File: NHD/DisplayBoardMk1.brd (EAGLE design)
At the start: 95.2 x 82.5 mm, 21 parts, among them K1 AQH2223

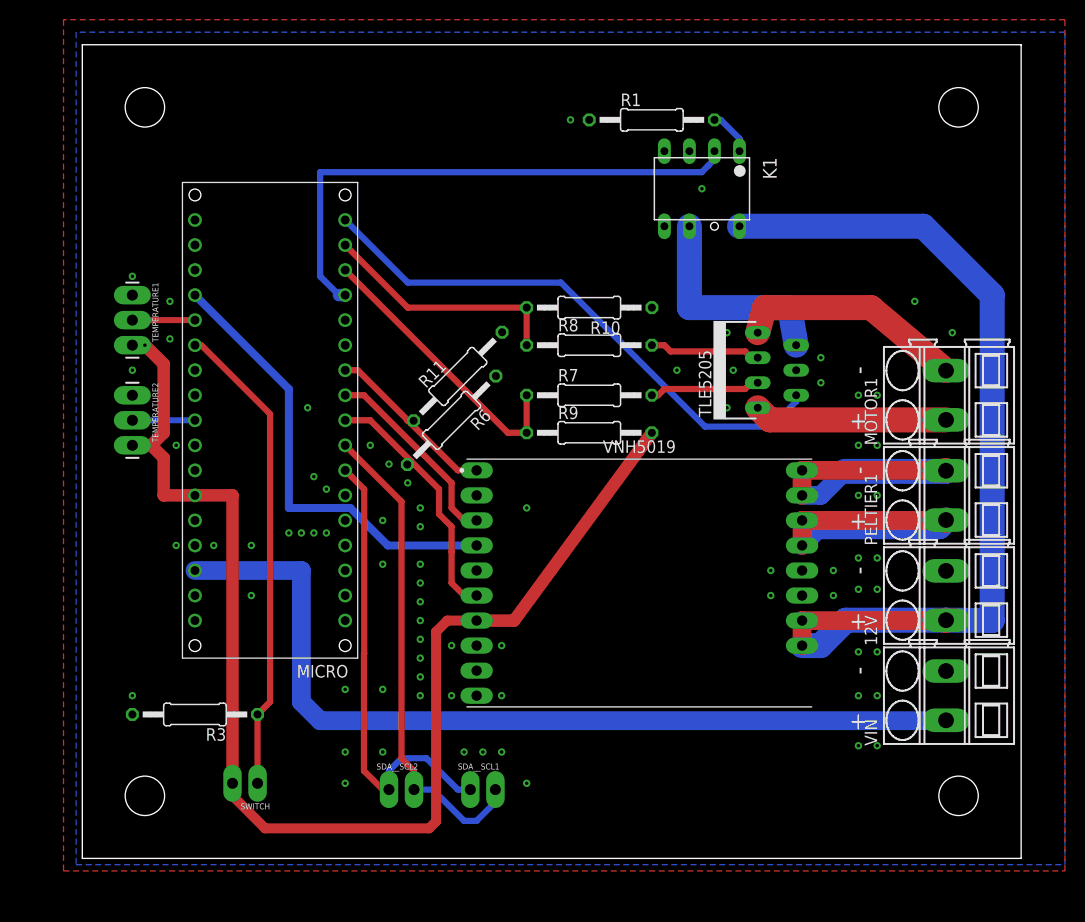
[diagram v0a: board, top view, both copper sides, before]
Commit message: Display Board. Attained old board files. Schematic organization.
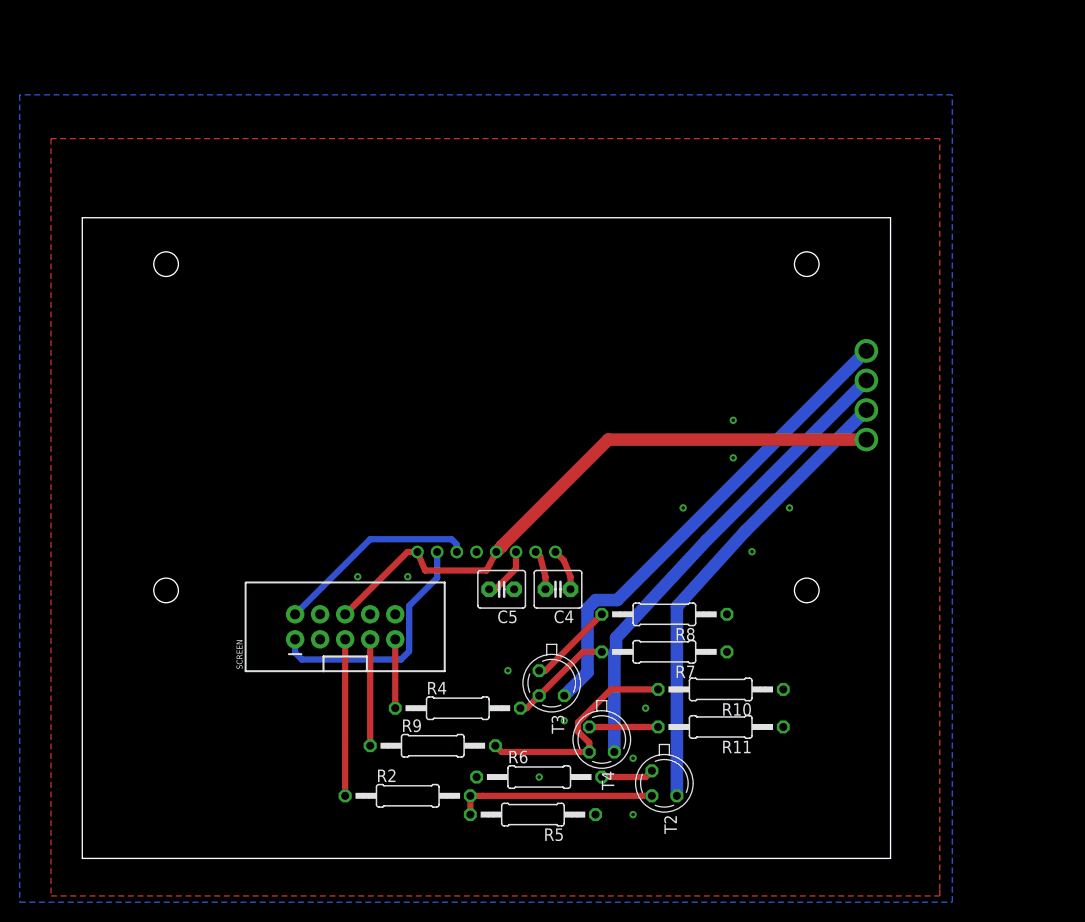
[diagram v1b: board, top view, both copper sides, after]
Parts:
- removed 12V, MOTOR1, PELTIER1, VIN: SMKDSP_1,5/2, con-phoenix-smkdsp:SMKDSP_1,5/2
- removed K1: AQH2223, relay:DIL07
- removed MICRO: ARDUINO_MICROFOOTPRINT, arduino-micro:ARDUINO-MICRO
- removed R1: 220, resistor:0207/12
- removed R3: 4.7k, resistor:0207/12
- removed SDA__SCL1, SDA__SCL2, SWITCH: (no value), SparkFun-Connectors:1X02_LONGPADS
- removed TEMPERATURE1, TEMPERATURE2: (no value), SparkFun-Connectors:1X03_LONGPADS
- removed TLE5205: TLE5205-2, infineon:P-TO220-7-11
- removed VNH5019: VNH5019VNH5019BOARD, GEMS:DIP3302W60P254L2400H500Q20B
- added C4, C5: 0.1uf, capacitor-wima:C2.5-4
- added R2, R4: 1k, resistor:0207/12
- added R5: 47k, resistor:0207/12
- added SCREEN: (no value), SparkFun-Connectors:2X5-SHROUDED
- added T2, T3, T4: 2N2222, transistor:TO18
- added U4: NHD‐C0220, GEMS:NHD-C0220
- R11, R6: value 47k -> 36
- R7: value 1k -> 47k
- R8: value 1k -> 36
- R9: value 47k -> 1k
- moved R11 44.4 mm to (64.8, 13.3), turned to 180 degrees
- moved R10 41.0 mm to (64.8, 17.1)
- moved R6 37.3 mm to (46.4, 8.26), turned to 0 degrees
- moved R9 35.5 mm to (35.6, 11.4)
- moved R8 28.3 mm to (59.1, 24.8), turned to 180 degrees
- moved R7 27.1 mm to (59.1, 21.0), turned to 180 degrees
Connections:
- removed net +12V: 12V.1, K1.8, VNH5019.VIN1, VNH5019.VIN2
- removed net +5V: MICRO.5V, R9.2, SWITCH.2, TEMPERATURE1.3, TEMPERATURE2.3, VNH5019.VDD
- removed net DOORSWITCH: MICRO.A2, R3.1, SWITCH.1
- removed net IN1: R7.2, TLE5205.3
- removed net IN2: R8.2, TLE5205.5
- removed net MOTOR-ENABLE: K1.2, MICRO.D9
- removed net MOTOR-ERRORFLAG: MICRO.D12, TLE5205.2
- removed net MOTOR-IN1: MICRO.D10, R7.1, R9.1
- removed net MOTOR-IN2: MICRO.D11, R10.2, R8.1
- removed net MOTOR-OUT1: MOTOR1.1, TLE5205.1
- removed net MOTOR-OUT2: MOTOR1.2, TLE5205.7
- removed net PELTIER-CURRENT: MICRO.A0, VNH5019.CS
- removed net PELTIER-INA: MICRO.D6, R11.1, VNH5019.INA
- removed net PELTIER-INB: MICRO.D4, R6.2, VNH5019.INB
- removed net PELTIER-OUTA: PELTIER1.2, VNH5019.OUTA1, VNH5019.OUTA2
- removed net PELTIER-OUTB: PELTIER1.1, VNH5019.OUTB1, VNH5019.OUTB2
- removed net PELTIER-PWM: MICRO.D5, VNH5019.PWM
- removed net POST-OPTO-DIODE: K1.1, R1.2
- removed net RELAY-TO-MOTORCONTROLLER: K1.6, TLE5205.6
- removed net SCL: MICRO.D3, SDA__SCL1.2, SDA__SCL2.2
- removed net SDA: MICRO.D2, SDA__SCL1.1, SDA__SCL2.1
- removed net TEMPERATURE1: MICRO.A1, TEMPERATURE1.2
- removed net TEMPERATURE2: MICRO.A5, TEMPERATURE2.2
- removed net VIN: MICRO.VIN, VIN.1
- new net 3V3: SCREEN.6, U4.1, U4.5, U4.A
- new net BLUE-NPN-BASE: R2.2, R5.2, T2.2
- new net BLUE-NPN-EMITTER: R6.2, T2.1
- new net GREEN-NPN-BASE: R10.2, R9.2, T4.2
- new net GREEN-NPN-EMITTER: R11.2, T4.1
- new net N$3: C5.2, U4.6
- new net RED-NPN-BASE: R4.2, R7.2, T3.2
- new net RED-NPN-EMITTER: R8.2, T3.1
- new net SCREEN-BLUE: T2.3, U4.BK
- new net SCREEN-BLUE-CONTROL: R2.1, SCREEN.5
- new net SCREEN-GREEN: T4.3, U4.GK
- new net SCREEN-GREEN-CONTROL: R9.1, SCREEN.7
- new net SCREEN-RED: T3.3, U4.RK
- new net SCREEN-RED-CONTROL: R4.1, SCREEN.9
- new net SCREEN-SCL: SCREEN.1, U4.2
- new net SCREEN-SDA: SCREEN.2, U4.3
- net GND: now also C5.1, R11.1, R5.1, R7.1, R8.1, SCREEN.10, SCREEN.3, SCREEN.4, SCREEN.8, U4.4; no longer 12V.2, MICRO.GND, MICRO.GND1, R1.1, R11.2, R3.2, TEMPERATURE1.1, TEMPERATURE2.1, TLE5205.4, VIN.2, VNH5019.GND1, VNH5019.GND2, VNH5019.GND3, VNH5019.GND4
- net N$21: now also C4.2, U4.7; no longer MICRO.D7
- net N$22: now also C4.1, U4.8; no longer MICRO.D8
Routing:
- net +5V: track 131.3 -> 0.00 mm, vias 1 -> 0
- net +12V: track 99.1 -> 0.00 mm
- net VIN: track 90.3 -> 0.00 mm
- net 3V3: track 0.00 -> 62.6 mm
- net MOTOR-ERRORFLAG: track 56.1 -> 0.00 mm
- net MOTOR-ENABLE: track 55.3 -> 0.00 mm
- net SCL: track 49.4 -> 0.00 mm
- net SCREEN-RED: track 0.00 -> 48.9 mm
- net DOORSWITCH: track 48.5 -> 0.00 mm
- net SCREEN-GREEN: track 0.00 -> 48.1 mm
- net SCREEN-BLUE: track 0.00 -> 46.9 mm
- net SDA: track 46.6 -> 0.00 mm
- net PELTIER-CURRENT: track 46.2 -> 0.00 mm
- net PELTIER-OUTB: track 32.8 -> 0.00 mm
- net PELTIER-OUTA: track 32.8 -> 0.00 mm
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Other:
- board size 95.2 x 82.5 mm -> 82 x 65 mm
- board text removed: "+"
- board text removed: "-"
